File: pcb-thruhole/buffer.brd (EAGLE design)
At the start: 98 x 24 mm, 16 parts, among them IC1 LF353N, IC2 LF353N, IC3 LF353N

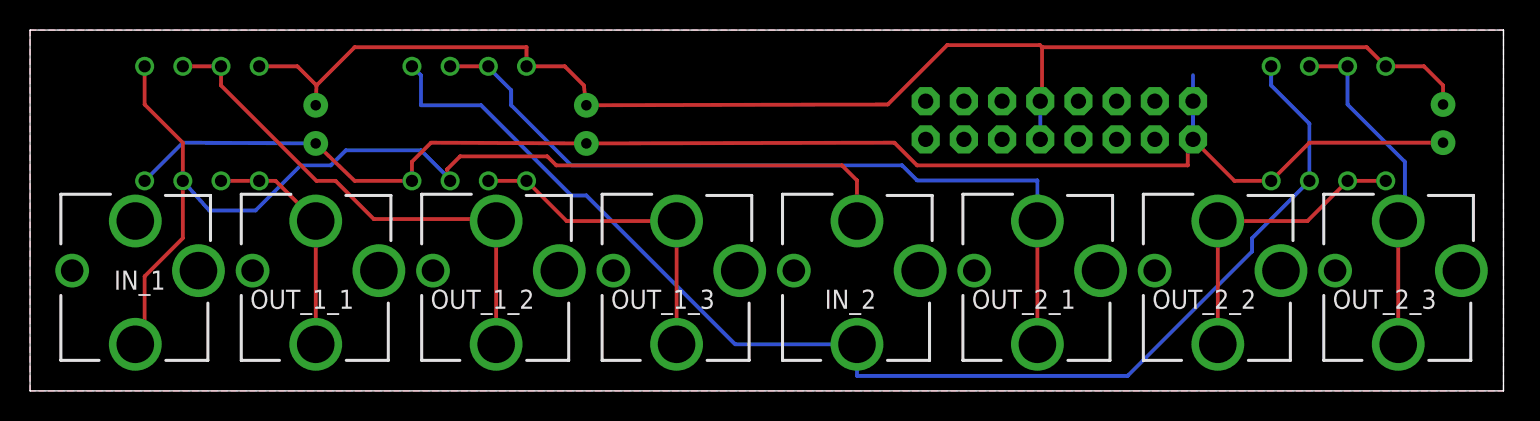
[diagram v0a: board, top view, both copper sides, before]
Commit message: moved some text off of holes, added url, made version 1.0
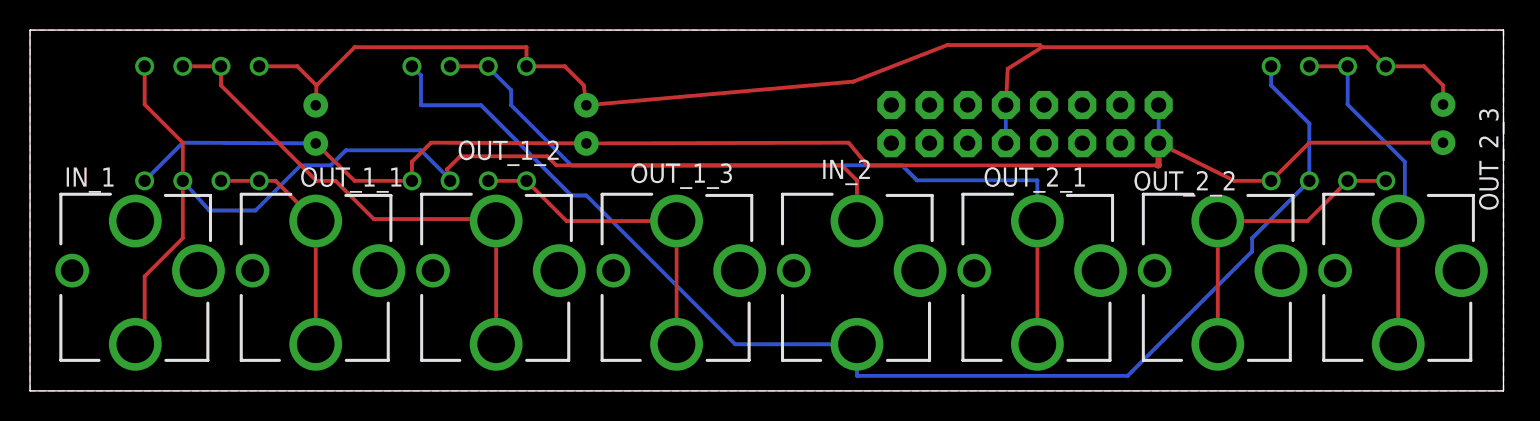
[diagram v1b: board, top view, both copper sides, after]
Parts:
- moved U$1 2.30 mm to (68.7, 17.7)
- moved U$6 1.63 mm to (52.1, 19.2)
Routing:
- net -12V: track 101.4 -> 96.6 mm
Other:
- board text added: "github.com/russellmcc/hexbuffer"
- board text added: "v1.0"
- board text removed: "alpha"
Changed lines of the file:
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@@
 <?xml version="1.0" encoding="utf-8"?>
 <!DOCTYPE eagle SYSTEM "eagle.dtd">
-<eagle version="6.1">
+<eagle version="6.4">
 <drawing>
 <settings>
@@
 <wire x1="98" y1="24" x2="0" y2="24" width="0" layer="20"/>
 <wire x1="0" y1="24" x2="0" y2="0" width="0" layer="20"/>
-<text x="41.91" y="18.03" size="1.778" layer="22" font="vector" ratio="15" rot="MR180">Hex Buffer</text>
-<text x="50.56" y="19.05" size="1.778" layer="22" font="vector" ratio="15" rot="MR0">alpha</text>
+<text x="38.354" y="17.776" size="1.778" layer="22" font="vector" ratio="15" rot="MR180">Hex Buffer</text>
+<text x="48.02" y="18.542" size="1.778" layer="22" font="vector" ratio="15" rot="MR0">v1.0</text>
+<text x="35.052" y="23.11" size="1.778" layer="22" font="vector" ratio="15" rot="MR180">github.com/russellmcc/hexbuffer</text>
 </plain>
 <attributes>
@@
 </class>
 </classes>
-<designrules>
+<designrules name="default">
 <description language="de">&lt;b&gt;EAGLE Design Rules&lt;/b&gt;
 &lt;p&gt;
@@
 <elements>
 <element name="IN_1" library="erthenvar" package="ERTHENVAR-JACK" value="AUDIO-JACKERTHENVAR" x="7" y="8" smashed="yes" rot="R180">
-<attribute name="NAME" x="9" y="8" size="1.27" layer="21" rot="R180"/>
+<attribute name="NAME" x="5.698" y="14.858" size="1.27" layer="21" rot="R180"/>
 </element>
 <element name="OUT_1_1" library="erthenvar" package="ERTHENVAR-JACK" value="AUDIO-JACKERTHENVAR" x="19" y="8" smashed="yes" rot="R180">
-<attribute name="NAME" x="21.54" y="6.73" size="1.27" layer="21" rot="R180"/>
+<attribute name="NAME" x="24.842" y="14.858" size="1.27" layer="21" rot="R180"/>
 </element>
 <element name="OUT_1_2" library="erthenvar" package="ERTHENVAR-JACK" value="AUDIO-JACKERTHENVAR" x="31" y="8" smashed="yes" rot="R180">
-<attribute name="NAME" x="33.54" y="6.73" size="1.27" layer="21" rot="R180"/>
+<attribute name="NAME" x="35.318" y="16.636" size="1.27" layer="21" rot="R180"/>
 </element>
 <element name="OUT_1_3" library="erthenvar" package="ERTHENVAR-JACK" value="AUDIO-JACKERTHENVAR" x="43" y="8" smashed="yes" rot="R180">
-<attribute name="NAME" x="45.54" y="6.73" size="1.27" layer="21" rot="R180"/>
+<attribute name="NAME" x="46.81" y="15.112" size="1.27" layer="21" rot="R180"/>
 </element>
 <element name="IN_2" library="erthenvar" package="ERTHENVAR-JACK" value="AUDIO-JACKERTHENVAR" x="55" y="8" smashed="yes" rot="R180">
-<attribute name="NAME" x="56.27" y="6.73" size="1.27" layer="21" rot="R180"/>
+<attribute name="NAME" x="56.016" y="15.366" size="1.27" layer="21" rot="R180"/>
 </element>
 <element name="OUT_2_1" library="erthenvar" package="ERTHENVAR-JACK" value="AUDIO-JACKERTHENVAR" x="67" y="8" smashed="yes" rot="R180">
-<attribute name="NAME" x="69.54" y="6.73" size="1.27" layer="21" rot="R180"/>
+<attribute name="NAME" x="70.302" y="14.858" size="1.27" layer="21" rot="R180"/>
 </element>
 <element name="OUT_2_2" library="erthenvar" package="ERTHENVAR-JACK" value="AUDIO-JACKERTHENVAR" x="79" y="8" smashed="yes" rot="R180">
-<attribute name="NAME" x="81.54" y="6.73" size="1.27" layer="21" rot="R180"/>
+<attribute name="NAME" x="80.27" y="14.604" size="1.27" layer="21" rot="R180"/>
 </element>
 <element name="OUT_2_3" library="erthenvar" package="ERTHENVAR-JACK" value="AUDIO-JACKERTHENVAR" x="91" y="8" smashed="yes" rot="R180">
-<attribute name="NAME" x="93.54" y="6.73" size="1.27" layer="21" rot="R180"/>
+<attribute name="NAME" x="96.394" y="18.864" size="1.27" layer="21" rot="R270"/>
 </element>
 <element name="IC1" library="linear" package="DIL08" value="LF353N" x="11.43" y="17.78" rot="MR0"/>
 <element name="IC2" library="linear" package="DIL08" value="LF353N" x="29.21" y="17.78" rot="MR0"/>
 <element name="IC3" library="linear" package="DIL08" value="LF353N" x="86.36" y="17.78" rot="MR0"/>
-<element name="U$1" library="eurorack" package="POWER_16" value="POWER_SIMPLE16" x="71" y="18" smashed="yes" rot="MR0"/>
+<element name="U$1" library="eurorack" package="POWER_16" value="POWER_SIMPLE16" x="68.714" y="17.746" smashed="yes" rot="MR0"/>
 <element name="C1" library="SparkFun" package="CAP-PTH-SMALL" value=".1uF" x="19" y="19" smashed="yes" rot="MR270">
 <attribute name="NAME" x="17.73" y="19.762" size="0.4064" layer="26" rot="MR270"/>
@@
 <attribute name="VALUE" x="95.504" y="18.796" size="0.4064" layer="28" rot="MR270"/>
 </element>
-<element name="U$6" library="SparkFun" package="OSHW-LOGO-S" value="" x="53.4" y="20.193" smashed="yes" rot="MR0"/>
+<element name="U$6" library="SparkFun" package="OSHW-LOGO-S" value="" x="52.13" y="19.177" smashed="yes" rot="MR0"/>
 </elements>
 <signals>
@@
 <contactref element="C2" pad="2"/>
 <contactref element="C3" pad="2"/>
-<wire x1="77.35" y1="19.27" x2="77.35" y2="16.73" width="0.254" layer="16"/>
-<wire x1="77.35" y1="16.73" x2="77.35" y2="21" width="0.254" layer="16"/>
+<wire x1="75.064" y1="19.016" x2="75.064" y2="16.476" width="0.254" layer="16"/>
 <wire x1="93.98" y1="16.51" x2="85.09" y2="16.51" width="0.254" layer="1"/>
 <wire x1="85.09" y1="16.51" x2="82.55" y2="13.97" width="0.254" layer="1"/>
 <wire x1="82.55" y1="13.97" x2="80.11" y2="13.97" width="0.254" layer="1"/>
-<wire x1="80.11" y1="13.97" x2="77.35" y2="16.73" width="0.254" layer="1"/>
+<wire x1="80.11" y1="13.97" x2="75.064" y2="16.476" width="0.254" layer="1"/>
 <wire x1="7.62" y1="13.97" x2="10.16" y2="16.51" width="0.254" layer="16"/>
 <wire x1="10.16" y1="16.51" x2="19" y2="16.46" width="0.254" layer="16"/>
@@
 <wire x1="25.4" y1="15.24" x2="26.67" y2="16.51" width="0.254" layer="1"/>
 <wire x1="26.67" y1="16.51" x2="37" y2="16.46" width="0.254" layer="1"/>
-<wire x1="37" y1="16.46" x2="57.49" y2="16.51" width="0.254" layer="1"/>
-<wire x1="57.49" y1="16.51" x2="59" y2="15" width="0.254" layer="1"/>
-<wire x1="59" y1="15" x2="77" y2="15" width="0.254" layer="1"/>
-<wire x1="77" y1="15" x2="77" y2="16.38" width="0.254" layer="1"/>
-<wire x1="77" y1="16.38" x2="77.35" y2="16.73" width="0.254" layer="1"/>
+<wire x1="37" y1="16.46" x2="54.442" y2="16.51" width="0.254" layer="1"/>
+<wire x1="54.442" y1="16.51" x2="55.698" y2="15" width="0.254" layer="1"/>
+<wire x1="55.698" y1="15" x2="74.968" y2="15" width="0.254" layer="1"/>
+<wire x1="74.968" y1="15" x2="75.064" y2="15" width="0.4064" layer="1"/>
+<wire x1="75.064" y1="15" x2="75.064" y2="16.476" width="0.4064" layer="1"/>
 </signal>
 <signal name="N$1">
@@
 <contactref element="C2" pad="1"/>
 <contactref element="C3" pad="1"/>
-<wire x1="67.19" y1="19.27" x2="67.19" y2="16.73" width="0.254" layer="16"/>
+<wire x1="64.904" y1="19.016" x2="64.904" y2="16.476" width="0.254" layer="16"/>
 <wire x1="93.98" y1="19.05" x2="93.98" y2="20.32" width="0.254" layer="1"/>
 <wire x1="93.98" y1="20.32" x2="92.71" y2="21.59" width="0.254" layer="1"/>
@@
 <wire x1="90.17" y1="21.59" x2="88.9" y2="22.86" width="0.254" layer="1"/>
 <wire x1="88.9" y1="22.86" x2="67.31" y2="22.86" width="0.254" layer="1"/>
-<wire x1="67.31" y1="22.86" x2="67.31" y2="19.39" width="0.254" layer="1"/>
-<wire x1="67.31" y1="19.39" x2="67.19" y2="19.27" width="0.254" layer="1"/>
+<wire x1="67.31" y1="22.86" x2="65.024" y2="21.422" width="0.254" layer="1"/>
+<wire x1="65.024" y1="21.422" x2="64.904" y2="19.016" width="0.254" layer="1"/>
 <wire x1="19.05" y1="20.32" x2="21.59" y2="22.86" width="0.254" layer="1"/>
 <wire x1="21.59" y1="22.86" x2="33.02" y2="22.86" width="0.254" layer="1"/>
 <wire x1="33.02" y1="22.86" x2="33.02" y2="21.59" width="0.254" layer="1"/>
-<wire x1="37" y1="19" x2="57.05" y2="19.05" width="0.254" layer="1"/>
-<wire x1="57.05" y1="19.05" x2="61" y2="23" width="0.254" layer="1"/>
+<wire x1="37" y1="19" x2="54.764" y2="20.574" width="0.254" layer="1"/>
+<wire x1="54.764" y1="20.574" x2="61" y2="23" width="0.254" layer="1"/>
 <wire x1="61" y1="23" x2="67.17" y2="23" width="0.254" layer="1"/>
 <wire x1="67.17" y1="23" x2="67.31" y2="22.86" width="0.254" layer="1"/>
